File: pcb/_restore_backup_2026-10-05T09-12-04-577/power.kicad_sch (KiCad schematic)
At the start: 5 parts, among them Y1 Crystal_GND24

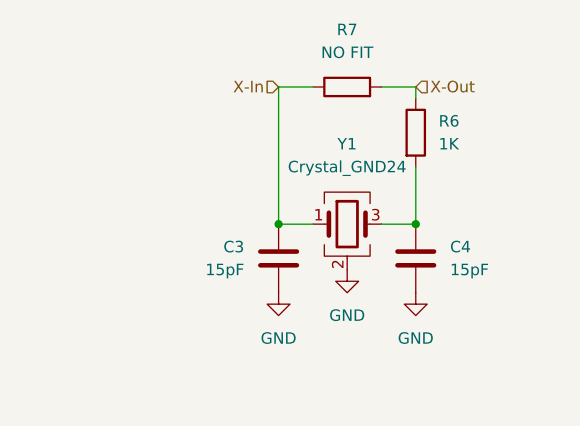
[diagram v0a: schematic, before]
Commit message: making the power delivery
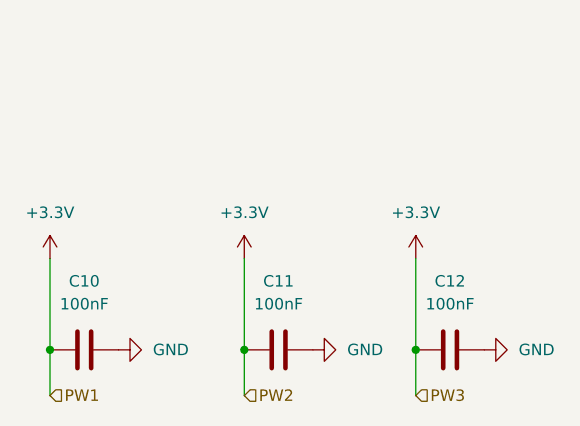
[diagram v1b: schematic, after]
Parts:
- removed C3, C4: 15pF, Package_SON:Winbond_USON-8-1EP_3x2mm_P0.5mm_EP0.2x1.6mm, symbol Device:C
- removed R6: 1K, Package_DIP:DIP-8_W7.62mm, symbol Device:R
- removed R7: NO FIT, symbol Device:R
- removed Y1: Crystal_GND24, symbol Device:Crystal_GND24
- added C10, C11, C12: 100nF, symbol Device:C
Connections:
- net GND: now also C10.2, C11.2, C12.2
- new net +3.3V: C10.1, C11.1, C12.1
